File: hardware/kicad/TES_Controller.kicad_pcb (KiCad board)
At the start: 2 copper layers, 64.1 x 89.3 mm, 77 parts

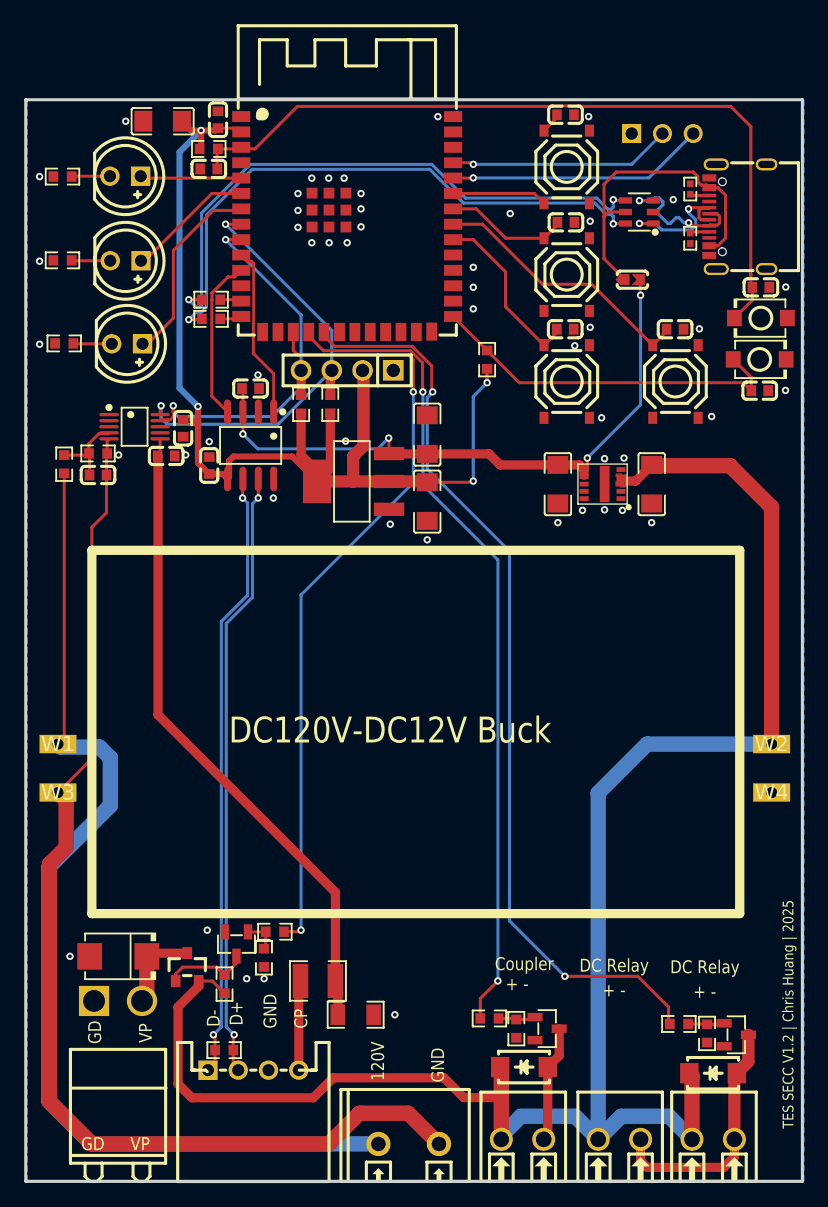
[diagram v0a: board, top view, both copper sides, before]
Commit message: Add the two TVS, and stop the copper pours from breaking connections
D9 (SMBJ130A) clamps the 120 V input, D10 (SMBJ13A) the 12 V rail. Both
reuse the SMBJ12A symbol and SMB footprint already in the library, so no new
parts were needed — only the value differs.

D9 goes at U10, the screw terminal where 120 V enters the board, not at W1
where the module's wires leave it. They are the same net, but a surge
arrives at U10 and there is 64 mm of track (~50 nH) between the two; a TVS
at W1 lets U10 rise well above the clamp, and R10 — a single 0603 rated 75 V
already sitting at 116 V — hangs off that end. It clamps to GND_BACK rather
than board ground so the surge current stays in the high-voltage loop.

13 V rather than 12 V on the rail: SMBJ12A's standoff voltage is exactly
12.0 V, so it would leak at the rail's own operating voltage once module
tolerance and ripple are included. (D3 on VP has the same issue and is worth
revisiting.)

Electrical changes are declared in tools/changes_v13.py rather than edited
in by hand, so verification survives them: the check is now "V1.3's netlist
plus the declared changes" against the board, still 226 connections and zero
difference. Each entry carries its reasoning.

The bigger find was that re-pouring kept breaking connections — a different
one or two each time. EasyEDA exports the small copper patch beside each pad
as its own zone, 233 of them at 0.01-0.05 mm2, and KiCad re-evaluates them
against its island rules on every refill. Deleting all 233 cost 3
connections to repair, which the repair pass handles. That also means every
refill the user does in the GUI would have broken something.

Three bugs in the new tooling, all found by DRC rather than by reading:
- Placement only tested courtyard overlap, so D9 landed with its 120 V pad
  0.047 mm from a 12 V track. Pad clearance is checked now, high-voltage
  rule included.
- A valid position is not a routable one: D9's first spot sat across the
  12 V trunk with no way around it. Pl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
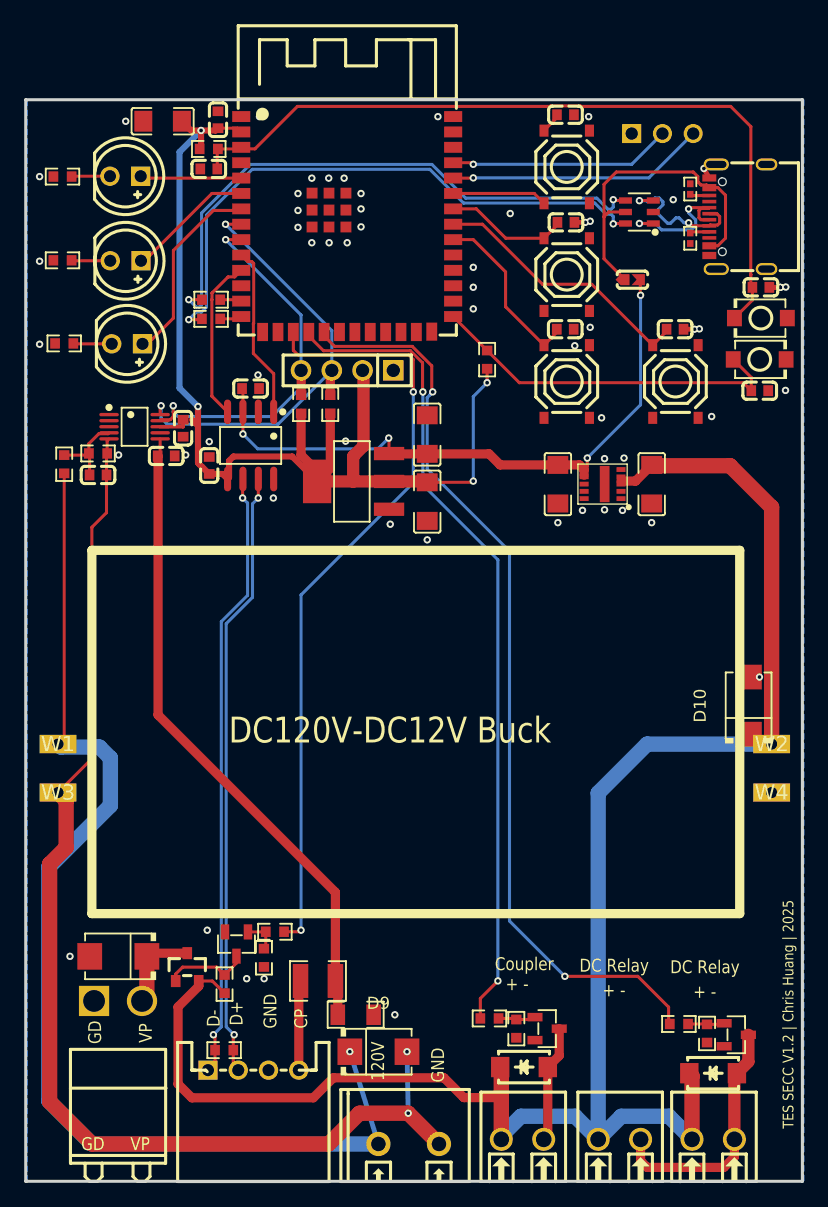
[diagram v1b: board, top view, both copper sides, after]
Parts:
- added D10: SMBJ13A, SMB_L4.6-W3.6-LS5.3-RD, F.Cu at (179.7, 110.0)
- added D9: SMBJ130A, SMB_L4.6-W3.6-LS5.3-RD, F.Cu at (149.1, 138.6)
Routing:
- net 120V: track 86.5 -> 94.5 mm, vias 0 -> 2
- net GND: track 0.00 -> 5.40 mm, vias 52 -> 58
- net GND_BACK: track 93.0 -> 98.1 mm, vias 0 -> 2
- net 5V: track 52.7 -> 55.2 mm
- net 12V: track 149.5 -> 151.6 mm
- removed copper zone on F.Cu, net 12V

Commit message: Move routing off the bottom layer to get a real ground plane
V1.3 put 649 mm of copper on the bottom — 120 V, 12 V, all three gate
drives, CAN, USB — so the bottom was never a ground plane, and ground had to
be patched together on top instead. With 62 SMD footprints up there that
patch came out as two dozen islands, which is why every refill stranded a
different handful of decoupling capacitors.

What makes the fix possible is the buck module's reserved area: 48.5 x 24 mm
with no components, restricting height but not copper, sitting between the
ESP32 above and the drivers and connectors below. At 0.4 mm pitch it takes
about 120 parallel tracks and only 18 nets need to cross.

| | before | after |
|---|---|---|
| bottom copper | 649 mm, 18 nets | 125 mm, longest run 18 mm |
| bottom ground pour | fragmented | **one polygon, 5302 mm2** (93% of the board) |
| top copper | 771 mm | 1300 mm |
| vias | 94 | 116 |

Every ground pad now vias straight down to that plane rather than hunting for
the top pour — 54 new stitching vias, and the shortest return path as a side
effect.

The router is an A* over a 0.15 mm grid rasterised from the board, two layers
deep, with bottom travel at 4x cost and a via at 12. The goal was never zero
bottom copper, which is not realistic here, but bottom copper too short to
cut the plane.

Four things it got wrong, each caught by DRC rather than by inspection:

- Single-layer routing failed 15 of 18 nets and sent one on a 195 mm detour.
- The grid is an approximation, so paths that A* accepted collided under
  KiCad's real geometry: 122 violations. Every segment is now re-checked
  against the exact shapes, and failures are blocked out and re-routed.
- Vias were placed without any clearance check at all. Stitching added 55 of
  them and 36 fresh violations with them. via_ok() now checks copper on both
  layers, hole-to-hole and hole-to-pad spacing, and the board edge.
- The high-voltage dilation is 0.9 mm at this grid, which erases the 0.255 mm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
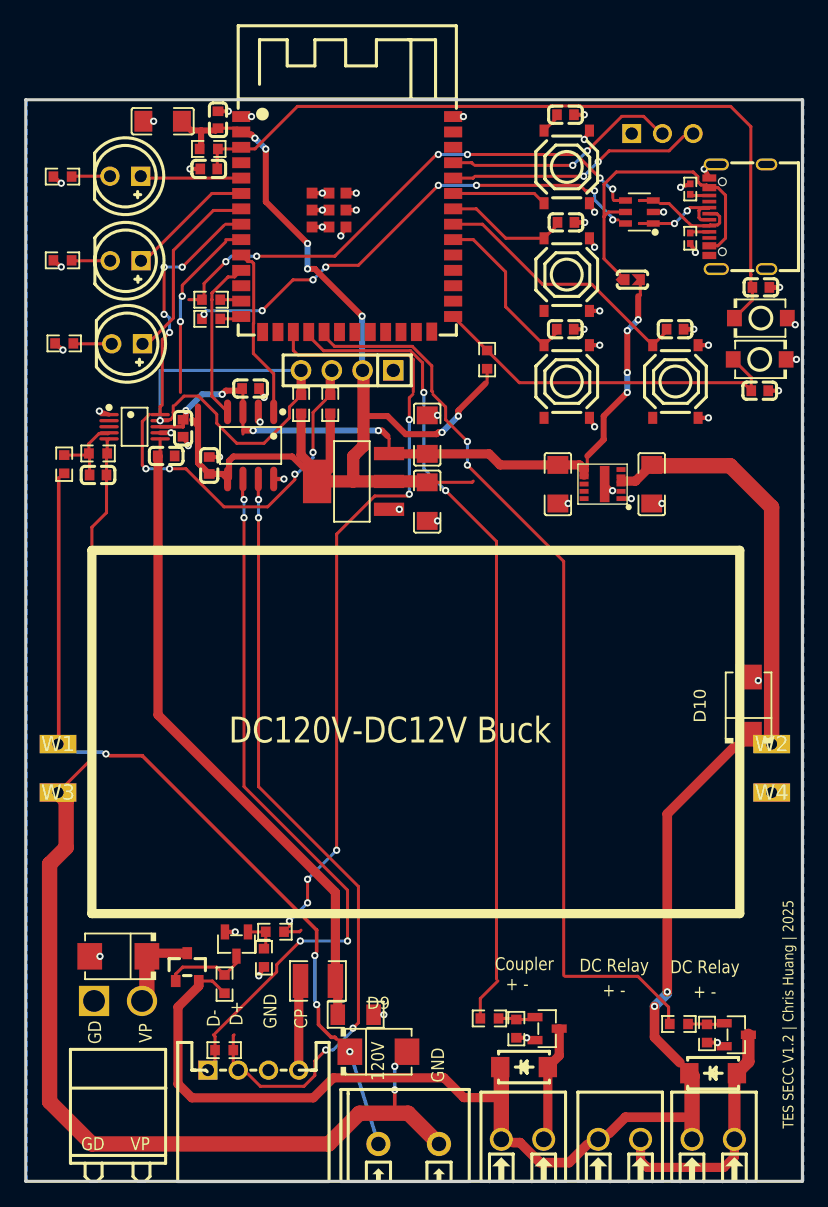
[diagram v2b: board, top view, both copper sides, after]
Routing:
- net GND: track 5.40 -> 52.2 mm, vias 58 -> 55
- net 120V: track 94.5 -> 63.0 mm, vias 2 -> 5
- net 12V: track 151.6 -> 131.8 mm, vias 0 -> 2
- net SDA: track 32.4 -> 49.7 mm, vias 2 -> 4
- net CANH: track 50.4 -> 63.9 mm, vias 2 -> 4
- net SCL: track 37.0 -> 49.6 mm, vias 2 -> 8
- net CANL: track 50.5 -> 59.3 mm, vias 2 -> 4
- net USB_DP_ESD: track 49.0 -> 40.4 mm, vias 2 -> 8
- net USB_DN_ESD: track 49.0 -> 43.1 mm, vias 2 -> 6
- net 5V: track 55.2 -> 59.2 mm, vias 4 -> 8
- net UD+: track 12.0 -> 8.06 mm
- net UD-: track 12.0 -> 8.27 mm, vias 2 -> 0
- net VDD33: track 93.8 -> 96.2 mm, vias 4 -> 7
- net GND_BACK: track 98.1 -> 96.5 mm
- net IO9: track 64.2 -> 65.6 mm, vias 2 -> 6
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
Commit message: Finish routing the restructured board and clear everything but courtyards
Every net is connected now — DRC reports zero unconnected items — and errors
are down from 63 to 21, all of them courtyard overlaps.

The fine-pitch pins were the hard part. U5 is an MSOP-10 rotated 90 degrees:
0.5 mm pitch leaves 0.22 mm between pads, so nothing can pass between them
and every pin has to escape past the end of its own pad. The grid router
cannot express that — dilation seals the pad in on all sides — so those pins
get a two-stage route: a short escape segment checked against real geometry,
then the maze from the escape point onward.

Two smaller router gaps showed up the same way. SCL failed at 0.25 mm and
routed immediately at 0.2 mm, so signal nets now retry narrower before
giving up; power and high-voltage nets do not, since their width is a
current and clearance requirement rather than a convenience. And the
gap-closer picked pad pairs without checking which fragment each belonged
to, so it kept re-adding the same track while the fragment count never
moved.

The worst bug was the gap-closer on GND. The grid does not contain zone
fills, so it saw a ground plane's pads as dozens of separate fragments and
"fixed" them with 27, 30 and 53 mm bottom-layer tracks — slicing apart the
plane this whole exercise was meant to create. 150 mm of that was reverted;
nets with a plane are now skipped there and left to the via stitcher.

The rest were judgement calls rather than bugs:

- Board edge clearance was KiCad's 0.5 mm default. Milled edges at JLCPCB
  allow 0.2 mm, so the rule is 0.3 mm, and the two stitching vias that still
  failed moved inward. My own check had been measuring to the outline's
  bounding box, which sits half a line width outside the real edge.
- The remaining edge violations are the USB-C's own pads against its own
  shell-leg slots, 0.156-0.210 mm. That is the connector's geometry, not
  routing: the pads cannot move, and V1.1 and V1.2 shipped with the same
  f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
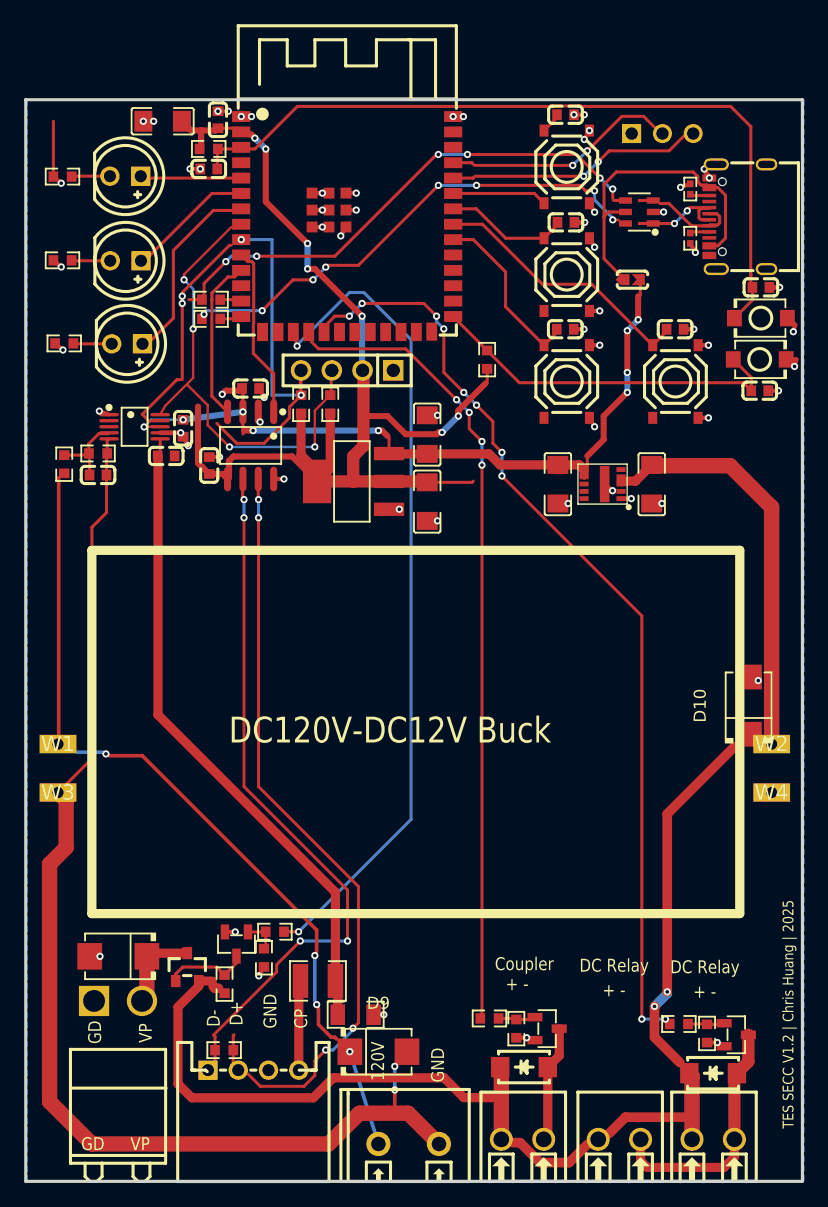
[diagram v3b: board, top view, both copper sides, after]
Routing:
- net SCL: track 49.6 -> 37.1 mm, vias 8 -> 4
- net GND: track 52.2 -> 57.9 mm, vias 55 -> 63
- net 5V: track 59.2 -> 62.3 mm, vias 8 -> 10
- net IO9: track 65.6 -> 68.0 mm, vias 6 -> 2
- net IO10: track 67.7 -> 65.6 mm, vias 2 -> 4
- net SDA: track 49.7 -> 47.9 mm
- net IO11: track 75.9 -> 77.1 mm, vias 2 -> 10
- net 12V: track 131.8 -> 130.9 mm
- net VDD33: track 96.2 -> 95.5 mm

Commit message: Clear the last DRC errors: zero errors, zero unconnected
Two placements actually needed moving, and neither was V1.3's fault — both
were mine. D10's pad sat directly on W2's wire pad, same net so not a short,
but nothing could be soldered to that pad afterwards. R21 overlapped CN2's
courtyard by 1.5 mm, deep enough that the resistor risked sitting under the
connector housing. Both moved 2 mm and their nets re-routed.

The remaining 20 courtyard overlaps are not assembly problems. What decides
whether two parts fit is the physical gap between their pads, and those
measure 0.356 to 3.671 mm — the tightest is well past JLCPCB's 0.2 mm
minimum, and V1.1 and V1.2 shipped with this placement. EasyEDA's footprints
simply carry generous courtyard margins, so neighbouring parts overlap
almost by definition. The real constraint is now a physical_clearance rule
at 0.3 mm, which DRC enforces; courtyard overlap drops to a warning so it
still reports without burying actual errors.

CAN was worth a second pass. After the clean-up CANH had ended up on the
bottom layer while CANL stayed on top — a differential pair split across
layers, with the loop area that implies. The top layer genuinely has no room
for both over their 45 mm run, so they now run together on the bottom:
parallel, equal length, 1.019 mm apart. The bottom pour still fills as a
single 5333 mm2 polygon, so the traces do not cut the plane.

Three tool bugs, all found by making things worse first:

- The dangling-stub cleaner deleted 21 "stubs" and broke 7 connections. A
  track endpoint that is not at a pad's centre can still be inside the pad;
  the test has to be geometric, not coordinate equality.
- The gap stitcher bridged every endpoint pair within 0.35 mm and added 207
  segments, wiring together tracks that merely bent near each other. It now
  only joins endpoints that are genuinely dangling.
- _pcb_relocate hit the same two SWIG limits as before, from opposite sides:
  iterating a collection after Remove(), a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
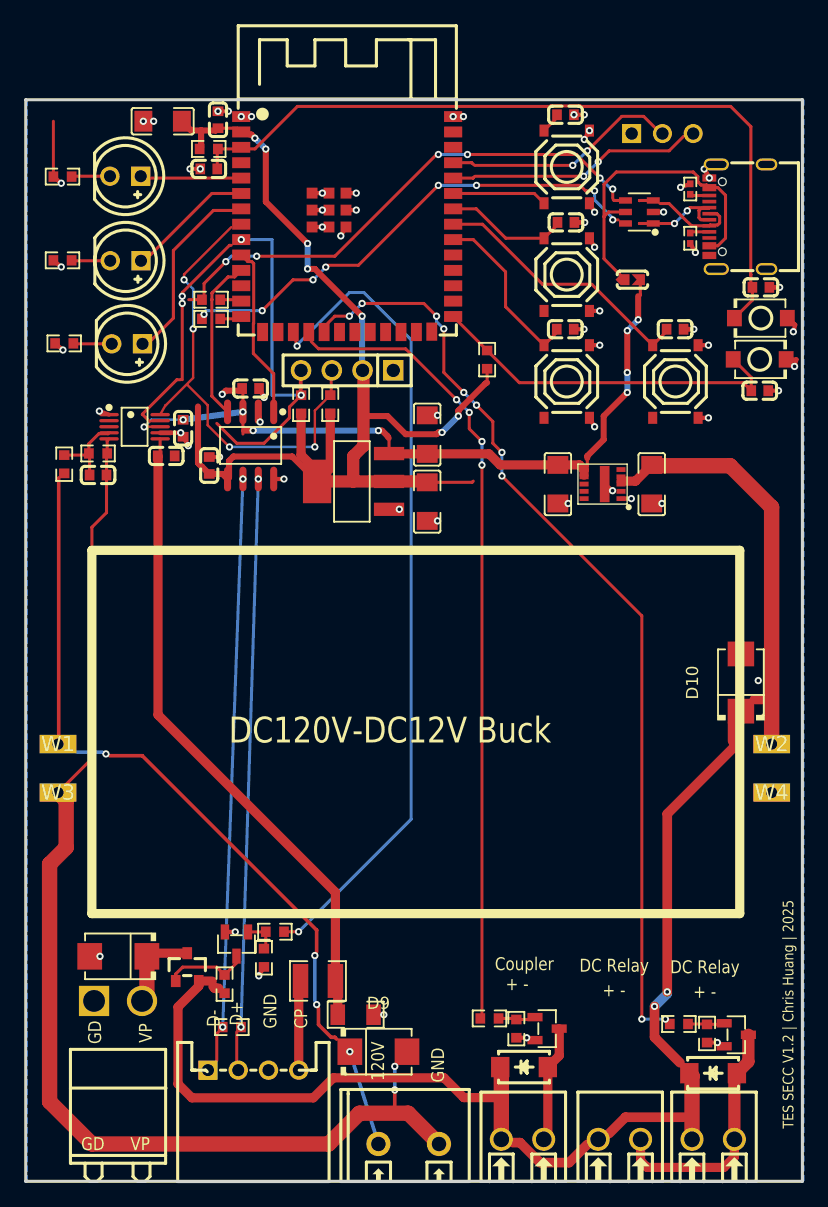
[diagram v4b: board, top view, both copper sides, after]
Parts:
- moved D10 2.01 mm to (179.1, 108.1)
- moved R21 2.01 mm to (137.0, 136.6)
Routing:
- net CANH: track 63.9 -> 47.7 mm, vias 4 -> 2
- net CANL: track 59.3 -> 47.8 mm, vias 4 -> 2
- net GND: track 57.9 -> 56.1 mm
